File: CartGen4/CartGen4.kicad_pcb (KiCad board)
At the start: 4 copper layers, 52.8 x 60.9 mm, 77 parts, among them J1 MEM2080-00-128-00-A, SW1 SW_Push, U1 TPS65266-1RHBR, U10 IS25WP080D-JNLE, U11 DS1391U-33+, U2 SN74LV1T34DCKR, U3 SIT8008BI-73-33E-33.333333G, U4 NXS0108BQX, U5 AS1C8M16PL-70BIN, U6 NXS0108BQX, U7 NXS0108BQX, U8 NXS0104BQX, U9 LFXP2-8E-5MN132C, Y1 FC-135R 32.7680KA-E5

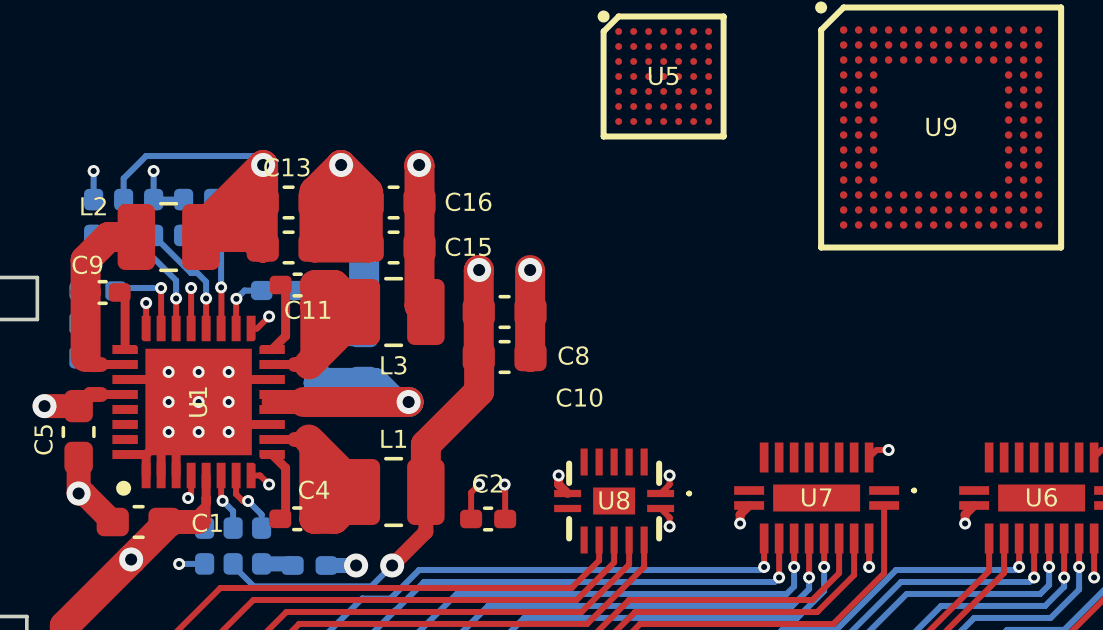
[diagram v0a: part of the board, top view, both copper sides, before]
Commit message: Updated to the latest JLCPCB capabilities
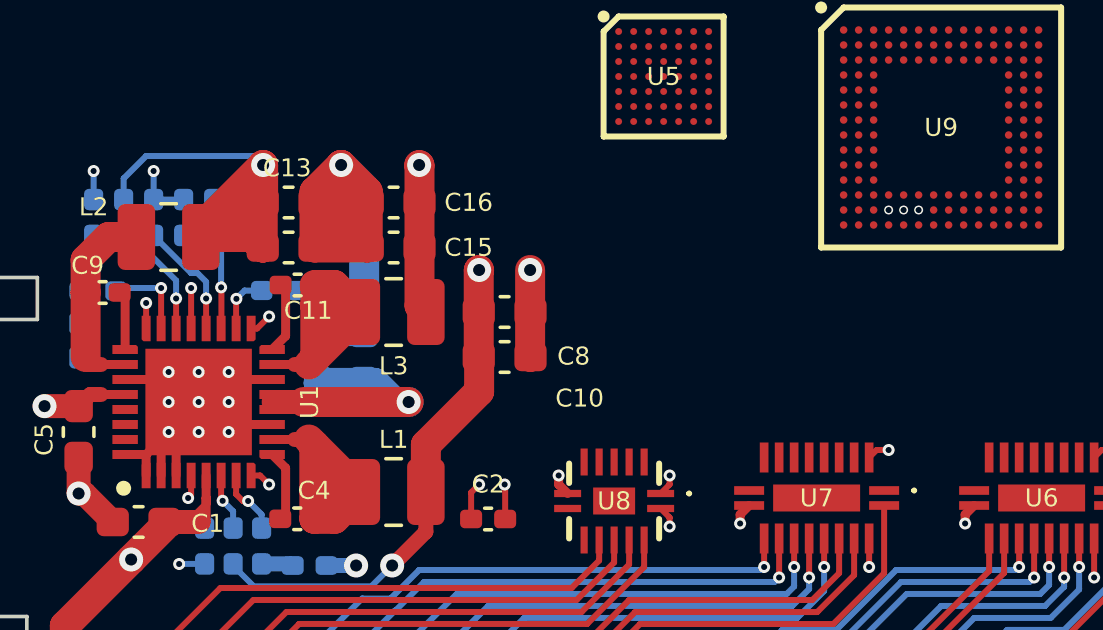
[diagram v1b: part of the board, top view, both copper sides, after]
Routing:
- net GND: vias 24 -> 25
- net GB_ADDR7: vias 0 -> 1
- net +3V3: vias 5 -> 6
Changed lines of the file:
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@@
     (property "Source" "SPEC")
     (attr smd)
-    (fp_text reference "U1" (at 0 0 90) (layer "F.SilkS")
+    (fp_text reference "U1" (at 0 3.7 90) (layer "F.SilkS")
       (effects (font (size 0.6 0.6) (thickness 0.125)))
     )
@@
   (via (at 46 82.8) (size 0.4) (drill 0.2) (layers "F.Cu" "B.Cu") (net 24))
   (via (at 80.05 86.8505) (size 0.4) (drill 0.2) (layers "F.Cu" "B.Cu") (free) (net 24))
+  (via (at 71 76.4) (size 0.3) (drill 0.2) (layers "F.Cu" "B.Cu") (net 24))
   (via (at 47 83.8) (size 0.4) (drill 0.2) (layers "F.Cu" "B.Cu") (net 24))
   (segment (start 46.3525 88.1975) (end 46.35 88.2) (width 0.2) (layer "B.Cu") (net 24))
@@
   (via (at 70 84.4) (size 0.4) (drill 0.2) (layers "F.Cu" "B.Cu") (free) (net 36))
   (via (at 54.35 74.9) (size 0.8) (drill 0.4) (layers "F.Cu" "B.Cu") (free) (net 36))
+  (via (at 70.5 76.4) (size 0.3) (drill 0.2) (layers "F.Cu" "B.Cu") (free) (net 36))
   (via (at 85 84.4) (size 0.4) (drill 0.2) (layers "F.Cu" "B.Cu") (free) (net 36))
   (segment (start 43 79.1525) (end 43.0525 79.1) (width 0.5) (layer "B.Cu") (net 37))
@@
   (segment (start 74.275 94.95) (end 74.275 92.275) (width 0.2) (layer "F.Cu") (net 79))
   (segment (start 74.275 92.275) (end 79.2 87.35) (width 0.2) (layer "F.Cu") (net 79))
+  (via (at 70 76.4) (size 0.3) (drill 0.2) (layers "F.Cu" "B.Cu") (net 128))
 )

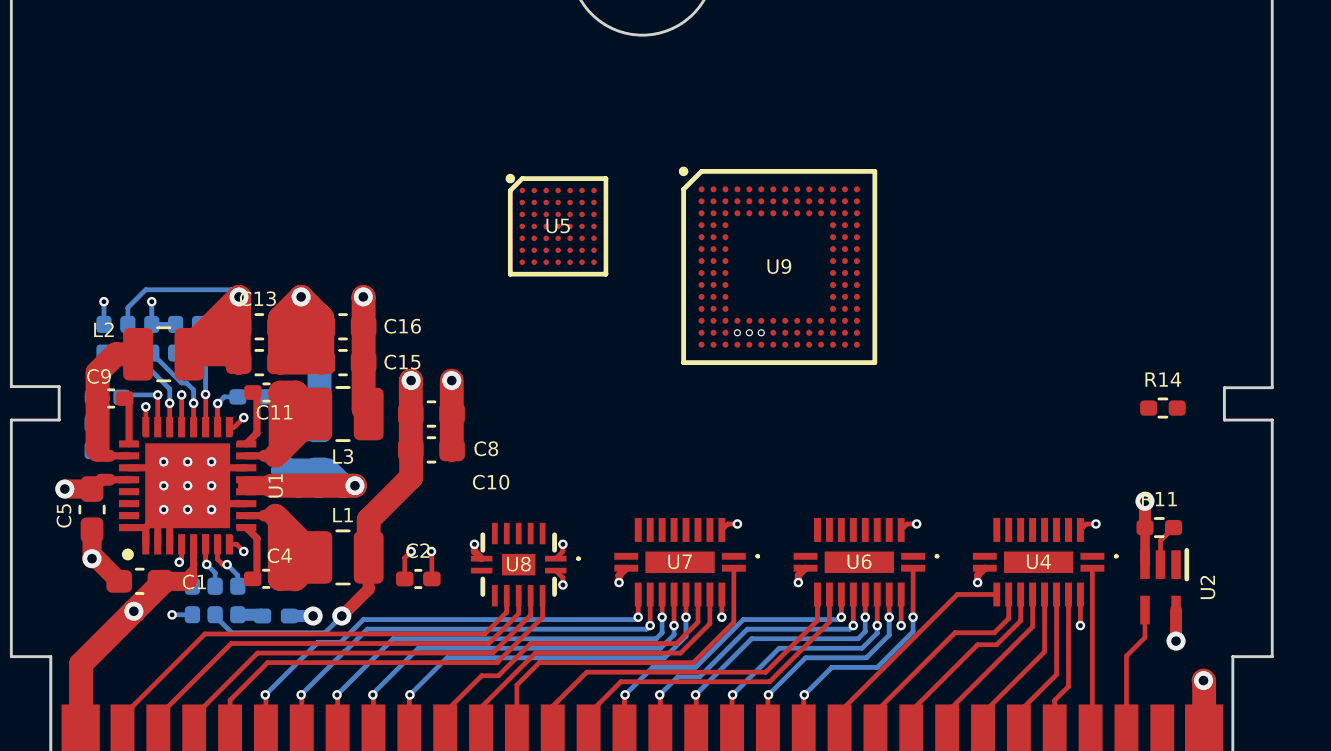
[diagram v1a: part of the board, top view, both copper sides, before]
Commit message: Started routing RAM
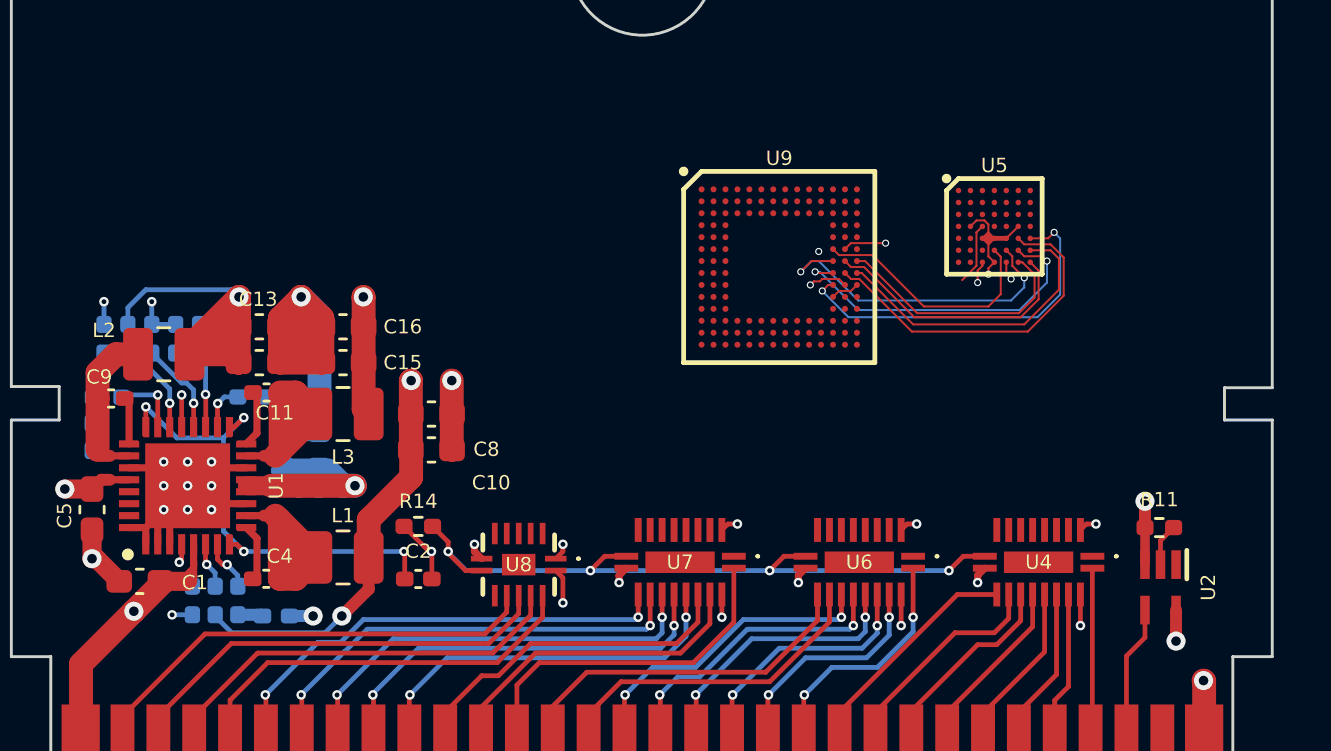
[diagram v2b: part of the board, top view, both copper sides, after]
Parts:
- moved R14 31.5 mm to (56.6, 84.5), turned to 180 degrees
- moved U5 18.2 mm to (80.8, 72.0)
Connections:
- U9 pad A5: RAM_CRE -> RAM_ADQ15
- U9 pad A6: RAM_UB# -> RAM_ADQ8
- U9 pad A7: RAM_LB# -> RAM_ADQ7
- U9 pad B6: RAM_CE1# -> RAM_ADQ3
- U9 pad B9: RAM_A18 -> RAM_ADQ1
- U9 pad C10: RAM_A17 -> RAM_ADQ2
- U9 pad C7: RAM_CE0# -> RAM_ADQ13
- U9 pad C9: RAM_A19 -> RAM_ADQ11
- U9 pad F12: RAM_ADQ15 -> RAM_CRE
- U9 pad G12: RAM_ADQ3 -> RAM_CE1#
- U9 pad G13: RAM_ADQ2 -> RAM_A17
- U9 pad G14: RAM_ADQ13 -> RAM_CE0#
- U9 pad H12: RAM_ADQ7 -> RAM_LB#
- U9 pad H13: RAM_ADQ8 -> RAM_UB#
- U9 pad H14: RAM_ADQ1 -> RAM_A18
- U9 pad J12: RAM_ADQ11 -> RAM_A19
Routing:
- net GB_BUS_EN: track 0.00 -> 29.7 mm, vias 0 -> 4
- net RAM_A19: track 0.00 -> 15.2 mm, vias 0 -> 2
- net RAM_UB#: track 0.00 -> 14.6 mm
- net RAM_LB#: track 0.00 -> 13.9 mm, vias 0 -> 2
- net RAM_CE1#: track 0.00 -> 13.8 mm, vias 0 -> 2
- net RAM_A18: track 0.00 -> 12.6 mm
- net RAM_A17: track 0.00 -> 11.1 mm
- net RAM_CE0#: track 0.00 -> 10.5 mm
- net RAM_CRE: track 0.00 -> 10.2 mm
- net GND: track 60.2 -> 67.4 mm
- net +1V8: track 17.0 -> 20.5 mm, vias 2 -> 5
- net RAM_ADQ12: track 0.00 -> 2.60 mm
- net +1V2: track 18.4 -> 20.1 mm, vias 1 -> 2
- net +3V3: track 8.08 -> 9.29 mm, vias 6 -> 5
- net +5V: track 32.3 -> 33.1 mm
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- added copper zone on In1.Cu, net +5V
- added copper zone on In2.Cu, net GND

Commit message: Figured out how to run the DAMN ram traces
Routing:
- net RAM_ADQ4: track 0.00 -> 2.40 mm
- net RAM_ADQ13: track 0.00 -> 2.07 mm
- net RAM_ADQ3: track 0.00 -> 1.90 mm
- net RAM_ADQ11: track 0.00 -> 1.85 mm
- net RAM_WE#: track 0.00 -> 1.55 mm
- net RAM_ADV#: track 0.00 -> 1.50 mm
- net RAM_ADQ6: track 0.00 -> 1.35 mm
- net GND: track 67.4 -> 68.7 mm
- net RAM_OE#: track 0.00 -> 1.20 mm
- net RAM_ADQ2: track 0.00 -> 1.15 mm
- net RAM_ADQ14: track 0.00 -> 1.08 mm
- net RAM_ADQ9: track 0.00 -> 1.02 mm
- net RAM_ADQ10: track 0.00 -> 1.00 mm
- net +1V8: track 20.5 -> 21.5 mm
- net RAM_ADQ5: track 0.00 -> 0.75 mm
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
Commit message: Started routing more ram, but I'd better sleep...
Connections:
- U9 pad D12: RAM_ADQ12 -> RAM_ADQ6
- U9 pad F14: RAM_ADQ6 -> RAM_ADQ12
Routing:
- net GND: track 68.7 -> 70.9 mm, vias 25 -> 29
- net RAM_CE1#: track 13.8 -> 11.7 mm
- net RAM_ADQ4: track 2.40 -> 3.61 mm
- net RAM_ADQ6: track 1.35 -> 2.11 mm, vias 0 -> 1
- net +1V8: track 21.5 -> 20.9 mm

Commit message: More RAM wire changes (i wanna cry)
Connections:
- U9 pad A10: RAM_ADV# -> RAM_ADQ6
- U9 pad A14: RAM_ADQ14 -> RAM_ADQ15
- U9 pad A2: RAM_WE# -> RAM_ADQ1
- U9 pad A3: RAM_OE# -> RAM_ADQ11
- U9 pad A5: RAM_ADQ15 -> RAM_ADQ8
- U9 pad A6: RAM_ADQ8 -> RAM_ADQ0
- U9 pad A7: RAM_ADQ7 -> RAM_ADQ3
- U9 pad A8: RAM_A21 -> RAM_ADQ10
- U9 pad A9: RAM_A16 -> RAM_ADQ14
- U9 pad B14: RAM_ADQ5 -> RAM_ADQ4
- U9 pad B6: RAM_ADQ3 -> RAM_ADQ2
- U9 pad B9: RAM_ADQ1 -> RAM_ADQ5
- U9 pad C10: RAM_ADQ2 -> RAM_ADQ13
- U9 pad C7: RAM_ADQ13 -> RAM_ADV#
- U9 pad C8: RAM_A20 -> RAM_ADQ9
- U9 pad C9: RAM_ADQ11 -> RAM_OE#
- U9 pad D12: RAM_ADQ6 -> RAM_WE#
- U9 pad D13: RAM_ADQ4 -> RAM_A20
- U9 pad D14: RAM_ADQ10 -> RAM_ADQ7
- U9 pad E12: RAM_ADQ0 -> RAM_A16
- U9 pad E14: RAM_ADQ9 -> RAM_A21
- U9 pad H13: RAM_UB# -> RAM_A19
- U9 pad J12: RAM_A19 -> RAM_UB#
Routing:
- net RAM_ADQ1: track 0.00 -> 22.1 mm
- net RAM_ADQ11: track 1.85 -> 21.8 mm
- net RAM_ADQ8: track 0.00 -> 18.8 mm
- net RAM_ADQ2: track 1.15 -> 18.8 mm
- net RAM_ADQ0: track 0.00 -> 16.6 mm
- net RAM_ADQ3: track 1.90 -> 16.7 mm
- net RAM_UB#: track 14.6 -> 0.71 mm, vias 0 -> 2
- net RAM_LB#: track 13.5 -> 0.71 mm
- net RAM_ADQ9: track 1.02 -> 13.6 mm
- net RAM_CE1#: track 11.7 -> 0.71 mm
- net RAM_ADQ10: track 1.00 -> 11.2 mm
- net RAM_ADQ5: track 0.75 -> 10.4 mm
- net RAM_CRE: track 10.2 -> 0.73 mm, vias 0 -> 2
- net RAM_ADQ13: track 2.07 -> 9.83 mm
- net RAM_ADQ14: track 1.08 -> 8.66 mm
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
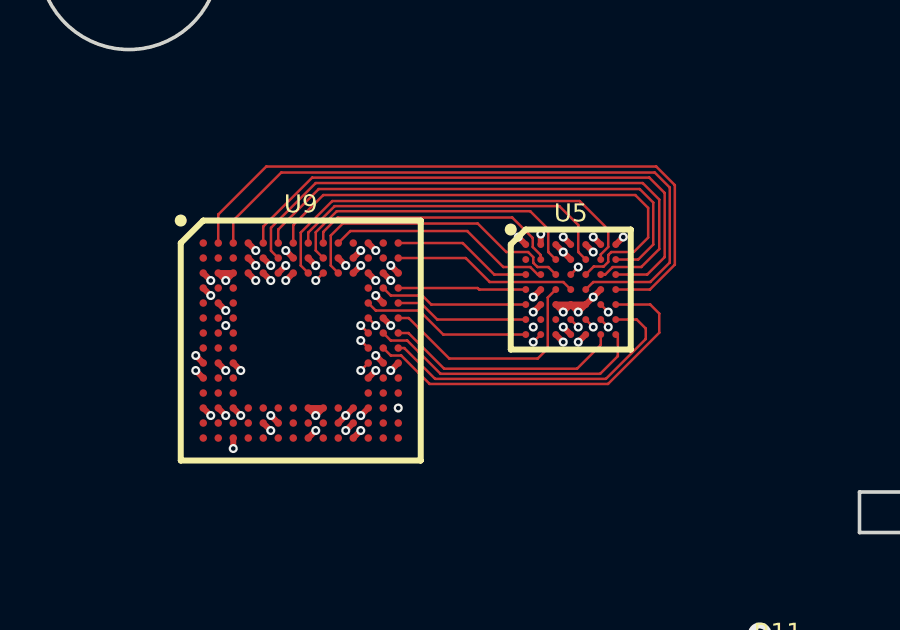
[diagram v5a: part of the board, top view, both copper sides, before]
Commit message: Wired all RAM signal wires (finally...)
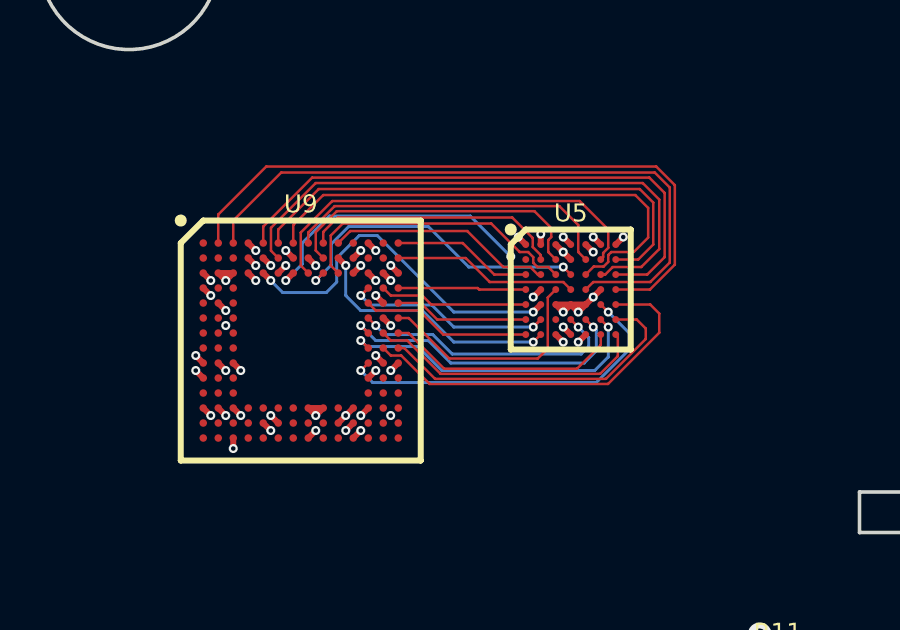
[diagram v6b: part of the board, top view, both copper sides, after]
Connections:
- U9 pad C5: RAM_WAIT -> RAM_ADV#
- U9 pad C7: RAM_ADV# -> RAM_WAIT
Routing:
- net RAM_ADV#: track 0.71 -> 11.9 mm
- net RAM_UB#: track 0.71 -> 11.8 mm
- net RAM_OE#: track 0.71 -> 10.7 mm
- net RAM_LB#: track 0.71 -> 10.6 mm
- net RAM_CE1#: track 0.71 -> 10.1 mm
- net RAM_WAIT: track 0.35 -> 9.71 mm, vias 1 -> 2
- net RAM_CRE: track 0.73 -> 9.12 mm
- net RAM_CLK: track 0.71 -> 8.60 mm
- net RAM_WE#: track 0.00 -> 6.89 mm, vias 1 -> 2

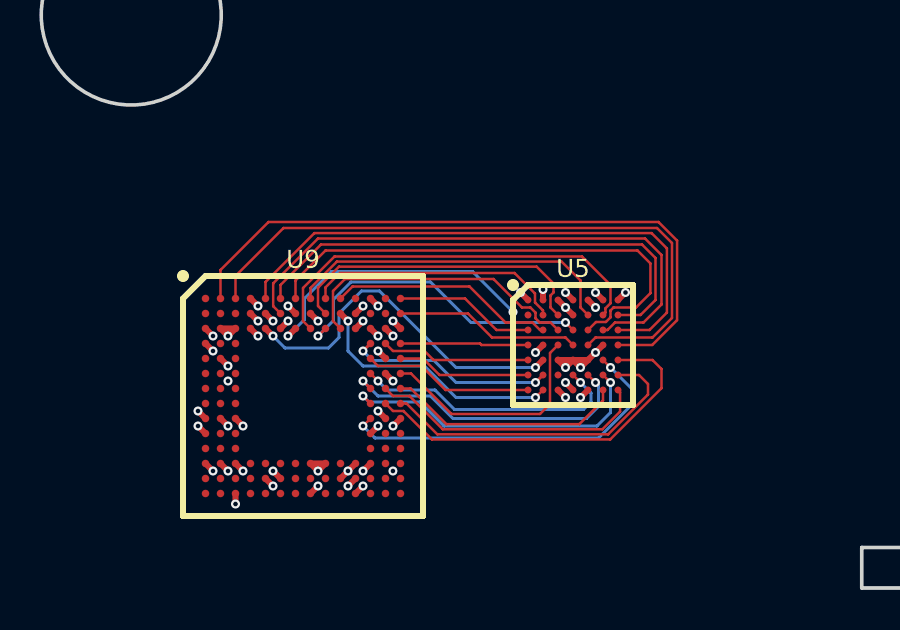
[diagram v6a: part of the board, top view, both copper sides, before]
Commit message: Adjusted RAM traces
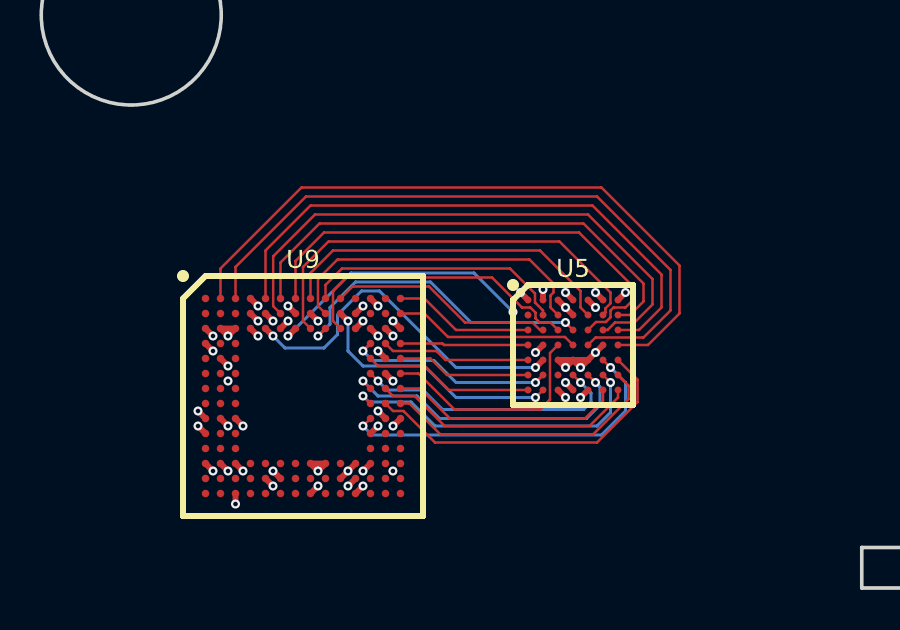
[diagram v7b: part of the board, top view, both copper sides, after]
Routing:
- net RAM_A19: track 12.6 -> 11.2 mm
- net RAM_A18: track 10.7 -> 9.46 mm
- net RAM_ADQ9: track 13.6 -> 14.3 mm
- net RAM_ADQ3: track 16.7 -> 16.2 mm
- net RAM_ADQ1: track 22.1 -> 22.6 mm
